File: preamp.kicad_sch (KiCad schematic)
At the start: 12 parts, among them SW1 PAD SW, U1 MAX4062

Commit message: re-annotate schematic
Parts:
- renumbered C3 to C10, C4 to C11, C1 to C8, C2 to C9, R1 to R28, R2 to R29, R3 to R30, R4 to R31, R5 to R32, SW1 to SW2, U1 to U5

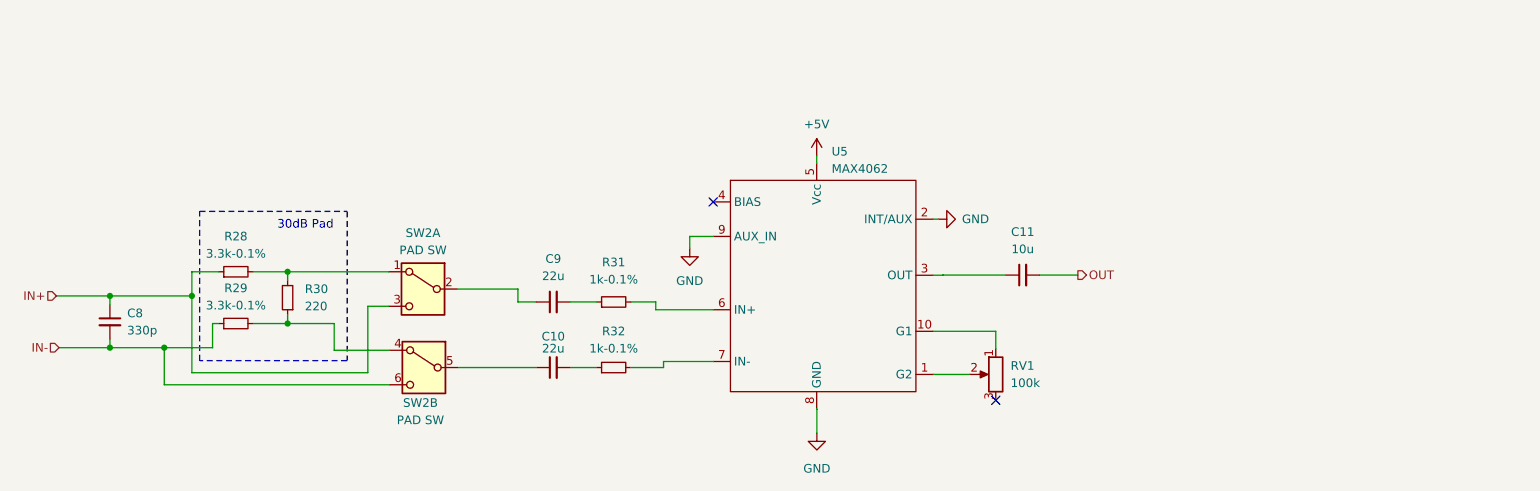
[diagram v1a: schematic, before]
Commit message: incorporate review feedback on schematic + pcb design
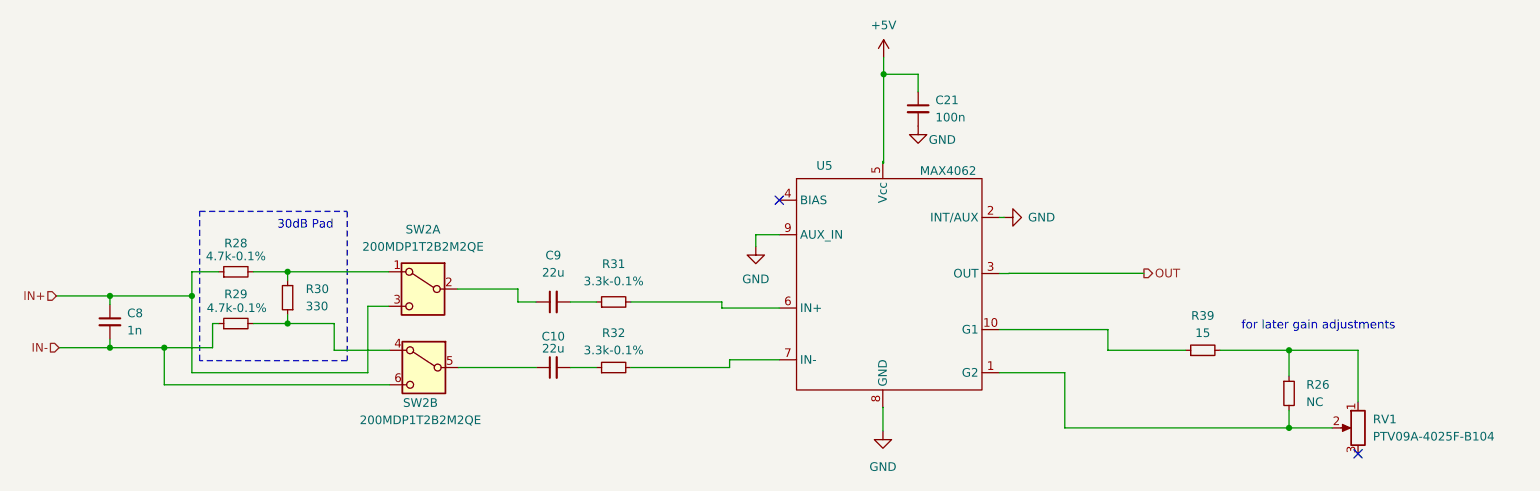
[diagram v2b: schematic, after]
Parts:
- removed C11: 10u, symbol Device:C_Small
- added C21: 100n, Capacitor_THT:C_Disc_D5.1mm_W3.2mm_P5.00mm, symbol Device:C_Small
- added R26: NC, Resistor_THT:R_Axial_DIN0207_L6.3mm_D2.5mm_P10.16mm_Horizontal, symbol Device:R_Small
- added R39: 15, Resistor_THT:R_Axial_DIN0207_L6.3mm_D2.5mm_P10.16mm_Horizontal, symbol Device:R_Small
- C10, C9: footprint (none) -> Capacitor_THT:C_Disc_D5.1mm_W3.2mm_P5.00mm
- C8: value 330p -> 1n; footprint (none) -> Capacitor_THT:C_Disc_D5.1mm_W3.2mm_P5.00mm
- R28, R29: value 3.3k-0.1% -> 4.7k-0.1%; footprint (none) -> Resistor_THT:R_Axial_DIN0207_L6.3mm_D2.5mm_P10.16mm_Horizontal
- R30: value 220 -> 330; footprint (none) -> Resistor_THT:R_Axial_DIN0207_L6.3mm_D2.5mm_P10.16mm_Horizontal
- R31, R32: value 1k-0.1% -> 3.3k-0.1%; footprint (none) -> Resistor_THT:R_Axial_DIN0207_L6.3mm_D2.5mm_P10.16mm_Horizontal
- RV1: value 100k -> PTV09A-4025F-B104; footprint (none) -> Potentiometer_THT:Potentiometer_Bourns_PTV09A-1_Single_Vertical
- SW2: value PAD SW -> 200MDP1T2B2M2QE; footprint (none) -> custom:SW_PUSH_E-Switch_200MDPxTxBxM2
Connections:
- net +5V: now also C21.1
- net GND: now also C21.2
- net OUT: now also U5.3 (OUT)
- net at RV1.1: now also R26.1, R39.2; no longer U5.10 (G1)
- net at RV1.2, U5.1 (G2): now also R26.2
- new net: R39.1, U5.10 (G1)
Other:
- note added: "for later gain adjustments"
- moved on the sheet: RV1, U5

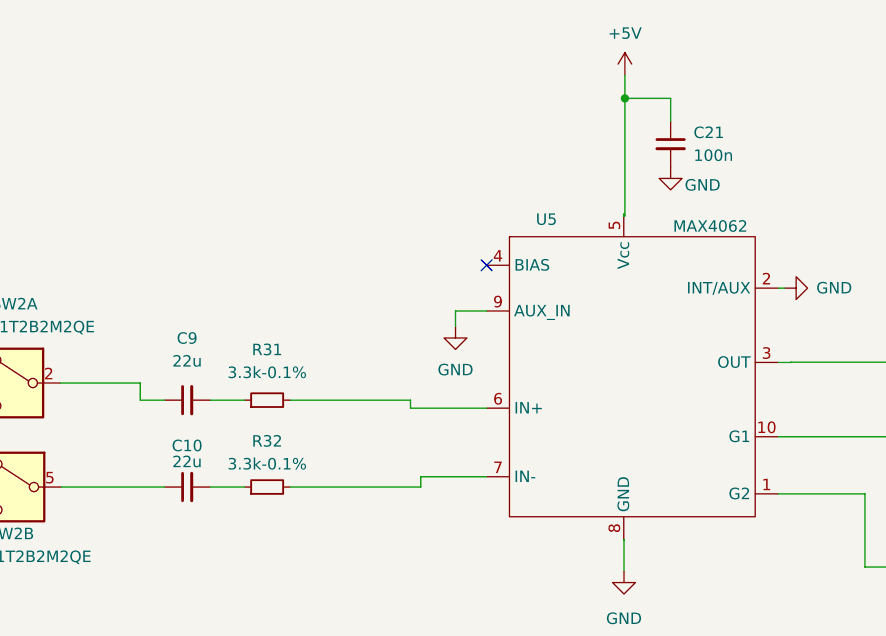
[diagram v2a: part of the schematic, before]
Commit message: 3.3V step down, fixed wrong CMV on balanced out, additional SMD footprints
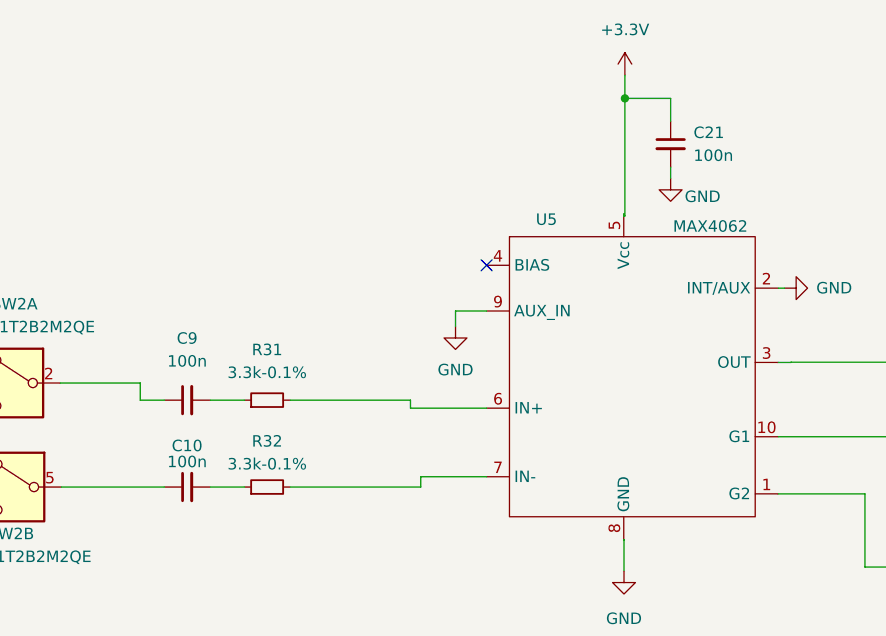
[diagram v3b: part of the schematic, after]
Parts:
- C10, C9: value 22u -> 100n
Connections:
- net +5V renamed +3.3V
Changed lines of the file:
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@@
+	(wire
+		(pts
+			(xy 185.42 55.88) (xy 185.42 54.61)
+		)
+		(stroke
+			(width 0)
+			(type default)
+		)
+	)
 	(wire
 		(pts
@@
 	(symbol
 		(lib_id "power:GND")
-		(at 185.42 54.61 0)
+		(at 185.42 55.88 0)
 		(unit 1)
 		(exclude_from_sim no)
@@
 		(dnp no)
 		(property "Reference" "#PWR023"
-			(at 185.42 60.96 0)
+			(at 185.42 62.23 0)
 			(effects
 				(font
@@
 		)
 		(property "Value" "GND"
-			(at 188.976 56.642 0)
+			(at 188.976 57.912 0)
 			(effects
 				(font
@@
 		)
 		(property "Footprint" ""
-			(at 185.42 54.61 0)
+			(at 185.42 55.88 0)
 			(effects
 				(font
@@
 		)
 		(property "Datasheet" ""
-			(at 185.42 54.61 0)
+			(at 185.42 55.88 0)
 			(effects
 				(font
@@
 		)
 		(property "Description" "Power symbol creates a global label with name \"GND\" , ground"
-			(at 185.42 54.61 0)
+			(at 185.42 55.88 0)
 			(effects
 				(font
@@
 				(path "/31073f88-a990-4ecc-8ab9-bb6b56c98e1e/5a710a45-03d0-4177-b57a-0573a00e8cb4"
 					(reference "R34")
-					(unit 1)
-				)
-			)
-		)
-	)
-	(symbol
-		(lib_id "power:+5V")
-		(at 180.34 44.45 0)
-		(unit 1)
-		(exclude_from_sim no)
-		(in_bom yes)
-		(on_board yes)
-		(dnp no)
-		(fields_autoplaced yes)
-		(property "Reference" "#PWR040"
-			(at 180.34 48.26 0)
-			(effects
-				(font
-					(size 1.27 1.27)
-				)
-				(hide yes)
-			)
-		)
-		(property "Value" "+5V"
-			(at 180.34 39.7764 0)
-			(effects
-				(font
-					(size 1.27 1.27)
-				)
-			)
-		)
-		(property "Footprint" ""
-			(at 180.34 44.45 0)
-			(effects
-				(font
-					(size 1.27 1.27)
-				)
-				(hide yes)
-			)
-		)
-		(property "Datasheet" ""
-			(at 180.34 44.45 0)
-			(effects
-				(font
-					(size 1.27 1.27)
-				)
-				(hide yes)
-			)
-		)
-		(property "Description" "Power symbol creates a global label with name \"+5V\""
-			(at 180.34 44.45 0)
-			(effects
-				(font
-					(size 1.27 1.27)
-				)
-				(hide yes)
-			)
-		)
-		(pin "1"
-		)
-		(instances
-			(project "spider2"
-				(path "/31073f88-a990-4ecc-8ab9-bb6b56c98e1e/ef17f1e3-6d4b-48c3-ada3-a0af083f4146"
-					(reference "#PWR040")
-					(unit 1)
-				)
-				(path "/31073f88-a990-4ecc-8ab9-bb6b56c98e1e/5a710a45-03d0-4177-b57a-0573a00e8cb4"
-					(reference "#PWR044")
 					(unit 1)
 				)
@@
 			)
 		)
-		(property "Value" "22u"
+		(property "Value" "100n"
 			(at 131.699 87.376 90)
 			(effects
@@
 			)
 		)
-		(property "Value" "22u"
+		(property "Value" "100n"
 			(at 131.7053 76.2 90)
 			(effects
@@
 					(unit 1)
 				)
+			)
+		)
+	)
+	(symbol
+		(lib_id "power:+3.3V")
+		(at 180.34 44.45 0)
+		(unit 1)
+		(exclude_from_sim no)
+		(in_bom yes)
+		(on_board yes)
+		(dnp no)
+		(fields_autoplaced yes)
+		(property "Reference" "#PWR040"
+			(at 180.34 48.26 0)
+			(effects
+				(font
+					(size 1.27 1.27)
+				)
+				(hide yes)
+			)
+		)
+		(property "Value" "+3.3V"
+			(at 180.34 39.37 0)
+			(effects
+				(font
+					(size 1.27 1.27)
+				)
+			)
+		)
+		(property "Footprint" ""
+			(at 180.34 44.45 0)
+			(effects
+				(font
+					(size 1.27 1.27)
+				)
+				(hide yes)
+			)
+		)
+		(property "Datasheet" ""
+			(at 180.34 44.45 0)
+			(effects
+				(font
+					(size 1.27 1.27)
+				)
+				(hide yes)
+			)
+		)
+		(property "Description" "Power symbol creates a global label with name \"+3.3V\""
+			(at 180.34 44.45 0)
+			(effects
+				(font
+					(size 1.27 1.27)
+				)
+				(hide yes)
+			)
+		)
+		(pin "1"
+		)
+		(instances
+			(project "spider2"
+				(path "/31073f88-a990-4ecc-8ab9-bb6b56c98e1e/ef17f1e3-6d4b-48c3-ada3-a0af083f4146"
+					(reference "#PWR040")
+					(unit 1)
+				)
+				(path "/31073f88-a990-4ecc-8ab9-bb6b56c98e1e/5a710a45-03d0-4177-b57a-0573a00e8cb4"
+					(reference "#PWR044")
+					(unit 1)
+				)

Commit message: jumper for switching input jacks between GND and BIAS
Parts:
- added C31: NC, Capacitor_SMD:C_0805_2012Metric_Pad1.18x1.45mm_HandSolder, symbol Device:C_Small
- added R42: NC, Resistor_SMD:R_0805_2012Metric_Pad1.20x1.40mm_HandSolder, symbol Device:R_Small
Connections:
- net GND: now also C31.2
- net at U5.4 (BIAS): now also C31.1, R42.2
- new net BIAS: R42.1
- no-connect marks 2 -> 1

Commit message: implement review feedback
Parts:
- R30: value 330 -> 330-1%
- R31, R32: value 3.3k-0.1% -> 4.7k-0.1%
- SW2: value 200MDP1T2B2M2QE -> 200MDP1T2B2M2
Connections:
- net +3.3V renamed +3.3VA
